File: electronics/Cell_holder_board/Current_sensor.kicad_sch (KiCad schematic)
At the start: 0 parts

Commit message: discord session with Johannes and Fabian, Schematic nearly done, all footprints fields filled
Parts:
- added C1: 220n 25V, Capacitor_SMD:C_0805_2012Metric, symbol Device:C
- added C2: 1n, Capacitor_SMD:C_0805_2012Metric, symbol Device:C
- added J2: Load_connector, TerminalBlock:TerminalBlock_bornier-2_P5.08mm, symbol Connector:Screw_Terminal_01x02
- added U10: ACS712xLCTR-20A, Package_SO:SOIC-8_3.9x4.9mm_P1.27mm, symbol Sensor_Current:ACS712xLCTR-20A
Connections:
- new net: C2.1, U10.6 (FILTER)
- new net +5V: C1.1, U10.8 (VCC)
- new net Current_signal: U10.7 (VIOUT)
- new net GND: C1.2, C2.2, U10.5 (GND)
- new net I_in: J2.2 (Pin_2), U10.1 (IP+), U10.2 (IP+)
- new net I_out: J2.1 (Pin_1), U10.3 (IP-), U10.4 (IP-)
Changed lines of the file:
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@@
 (kicad_sch (version 20230121) (generator eeschema)
   (paper "A4")
+  (wire (pts (xy 82.55 44.45) (xy 87.63 44.45))
+    (stroke (width 0) (type default))
+  )
+  (hierarchical_label "I_in" (shape bidirectional) (at 41.91 39.37 0) (fields_autoplaced)
+    (effects (font (size 1.27 1.27)) (justify left))
+  )
+  (hierarchical_label "I_out" (shape bidirectional) (at 41.91 41.91 0) (fields_autoplaced)
+    (effects (font (size 1.27 1.27)) (justify left))
+  )
+  (hierarchical_label "I_out" (shape bidirectional) (at 62.23 46.99 180) (fields_autoplaced)
+    (effects (font (size 1.27 1.27)) (justify right))
+  )
+  (hierarchical_label "I_in" (shape bidirectional) (at 62.23 36.83 180) (fields_autoplaced)
+    (effects (font (size 1.27 1.27)) (justify right))
+  )
+  (hierarchical_label "Current_signal" (shape output) (at 82.55 41.91 0) (fields_autoplaced)
+    (effects (font (size 1.27 1.27)) (justify left))
+  )
+  (symbol (lib_id "power:GND") (at 72.39 52.07 0) (unit 1)
+    (in_bom yes) (on_board yes) (dnp no) (fields_autoplaced)
+    (property "Reference" "#PWR021" (at 72.39 58.42 0)
+      (effects (font (size 1.27 1.27)) hide)
+    )
+    (property "Value" "GND" (at 72.39 57.15 0)
+      (effects (font (size 1.27 1.27)))
+    )
+    (property "Footprint" "" (at 72.39 52.07 0)
+      (effects (font (size 1.27 1.27)) hide)
+    )
+    (property "Datasheet" "" (at 72.39 52.07 0)
+      (effects (font (size 1.27 1.27)) hide)
+    )
+    (pin "1")
+    (instances
+      (project "Cell_holder_board"
+        (path "/c2697d40-f04f-4888-9ae9-ce0b7f222632/d1e5a9a1-ef5e-4043-b331-33dbe5a7732b"
+          (reference "#PWR021") (unit 1)
+        )
+      )
+    )
+  )
+  (symbol (lib_id "Device:C") (at 87.63 48.26 0) (unit 1)
+    (in_bom yes) (on_board yes) (dnp no) (fields_autoplaced)
+    (property "Reference" "C2" (at 91.44 47.625 0)
+      (effects (font (size 1.27 1.27)) (justify left))
+    )
+    (property "Value" "1n" (at 91.44 50.165 0)
+      (effects (font (size 1.27 1.27)) (justify left))
+    )
+    (property "Footprint" "Capacitor_SMD:C_0805_2012Metric" (at 88.5952 52.07 0)
+      (effects (font (size 1.27 1.27)) hide)
+    )
+    (property "Datasheet" "~" (at 87.63 48.26 0)
+      (effects (font (size 1.27 1.27)) hide)
+    )
+    (pin "1")
+    (pin "2")
+    (instances
+      (project "Cell_holder_board"
+        (path "/c2697d40-f04f-4888-9ae9-ce0b7f222632/d1e5a9a1-ef5e-4043-b331-33dbe5a7732b"
+          (reference "C2") (unit 1)
+        )
+      )
+    )
+  )
+  (symbol (lib_id "Device:C") (at 105.41 41.91 0) (unit 1)
+    (in_bom yes) (on_board yes) (dnp no) (fields_autoplaced)
+    (property "Reference" "C1" (at 109.22 41.275 0)
+      (effects (font (size 1.27 1.27)) (justify left))
+    )
+    (property "Value" "220n 25V" (at 109.22 43.815 0)
+      (effects (font (size 1.27 1.27)) (justify left))
+    )
+    (property "Footprint" "Capacitor_SMD:C_0805_2012Metric" (at 106.3752 45.72 0)
+      (effects (font (size 1.27 1.27)) hide)
+    )
+    (property "Datasheet" "~" (at 105.41 41.91 0)
+      (effects (font (size 1.27 1.27)) hide)
+    )
+    (pin "1")
+    (pin "2")
+    (instances
+      (project "Cell_holder_board"
+        (path "/c2697d40-f04f-4888-9ae9-ce0b7f222632/d1e5a9a1-ef5e-4043-b331-33dbe5a7732b"
+          (reference "C1") (unit 1)
+        )
+      )
+    )
+  )
+  (symbol (lib_id "power:GND") (at 87.63 52.07 0) (unit 1)
+    (in_bom yes) (on_board yes) (dnp no) (fields_autoplaced)
+    (property "Reference" "#PWR023" (at 87.63 58.42 0)
+      (effects (font (size 1.27 1.27)) hide)
+    )
+    (property "Value" "GND" (at 87.63 57.15 0)
+      (effects (font (size 1.27 1.27)))
+    )
+    (property "Footprint" "" (at 87.63 52.07 0)
+      (effects (font (size 1.27 1.27)) hide)
+    )
+    (property "Datasheet" "" (at 87.63 52.07 0)
+      (effects (font (size 1.27 1.27)) hide)
+    )
+    (pin "1")
+    (instances
+      (project "Cell_holder_board"
+        (path "/c2697d40-f04f-4888-9ae9-ce0b7f222632/d1e5a9a1-ef5e-4043-b331-33dbe5a7732b"
+          (reference "#PWR023") (unit 1)
+        )
+      )
+    )
+  )
+  (symbol (lib_id "power:GND") (at 105.41 45.72 0) (unit 1)
+    (in_bom yes) (on_board yes) (dnp no) (fields_autoplaced)
+    (property "Reference" "#PWR025" (at 105.41 52.07 0)
+      (effects (font (size 1.27 1.27)) hide)
+    )
+    (property "Value" "GND" (at 105.41 50.8 0)
+      (effects (font (size 1.27 1.27)))
+    )
+    (property "Footprint" "" (at 105.41 45.72 0)
+      (effects (font (size 1.27 1.27)) hide)
+    )
+    (property "Datasheet" "" (at 105.41 45.72 0)
+      (effects (font (size 1.27 1.27)) hide)
+    )
+    (pin "1")
+    (instances
+      (project "Cell_holder_board"
+        (path "/c2697d40-f04f-4888-9ae9-ce0b7f222632/d1e5a9a1-ef5e-4043-b331-33dbe5a7732b"
+          (reference "#PWR025") (unit 1)
+        )
+      )
+    )
+  )
+  (symbol (lib_id "power:+5V") (at 72.39 31.75 0) (unit 1)
+    (in_bom yes) (on_board yes) (dnp no) (fields_autoplaced)
+    (property "Reference" "#PWR022" (at 72.39 35.56 0)
+      (effects (font (size 1.27 1.27)) hide)
+    )
+    (property "Value" "+5V" (at 72.39 27.94 0)
+      (effects (font (size 1.27 1.27)))
+    )
+    (property "Footprint" "" (at 72.39 31.75 0)
+      (effects (font (size 1.27 1.27)) hide)
+    )
+    (property "Datasheet" "" (at 72.39 31.75 0)
+      (effects (font (size 1.27 1.27)) hide)
+    )
+    (pin "1")
+    (instances
+      (project "Cell_holder_board"
+        (path "/c2697d40-f04f-4888-9ae9-ce0b7f222632/d1e5a9a1-ef5e-4043-b331-33dbe5a7732b"
+          (reference "#PWR022") (unit 1)
+        )
+      )
+    )
+  )
+  (symbol (lib_id "power:+5V") (at 105.41 38.1 0) (unit 1)
+    (in_bom yes) (on_board yes) (dnp no) (fields_autoplaced)
+    (property "Reference" "#PWR024" (at 105.41 41.91 0)
+      (effects (font (size 1.27 1.27)) hide)
+    )
+    (property "Value" "+5V" (at 105.41 34.29 0)
+      (effects (font (size 1.27 1.27)))
+    )
+    (property "Footprint" "" (at 105.41 38.1 0)
+      (effects (font (size 1.27 1.27)) hide)
+    )
+    (property "Datasheet" "" (at 105.41 38.1 0)
+      (effects (font (size 1.27 1.27)) hide)
+    )
+    (pin "1")
+    (instances
+      (project "Cell_holder_board"
+        (path "/c2697d40-f04f-4888-9ae9-ce0b7f222632/d1e5a9a1-ef5e-4043-b331-33dbe5a7732b"
+          (reference "#PWR024") (unit 1)
+        )
+      )
+    )
+  )
+  (symbol (lib_id "Sensor_Current:ACS712xLCTR-20A") (at 72.39 41.91 0) (unit 1)
+    (in_bom yes) (on_board yes) (dnp no) (fields_autoplaced)
+    (property "Reference" "U10" (at 74.3459 30.48 0)
+      (effects (font (size 1.27 1.27)) (justify left))
+    )
+    (property "Value" "ACS712xLCTR-20A" (at 74.3459 33.02 0)
+      (effects (font (size 1.27 1.27)) (justify left))
+    )
+    (property "Footprint" "Package_SO:SOIC-8_3.9x4.9mm_P1.27mm" (at 74.93 50.8 0)
+      (effects (font (size 1.27 1.27) italic) (justify left) hide)
+    )
+    (property "Datasheet" "http://www.allegromicro.com/~/media/Files/Datasheets/ACS712-Datasheet.ashx?la=en" (at 72.39 41.91 0)
+      (effects (font (size 1.27 1.27)) hide)
+    )
+    (pin "1")
+    (pin "2")
+    (pin "3")
+    (pin "4")
+    (pin "5")
+    (pin "6")
+    (pin "7")
+    (pin "8")
+    (instances
+      (project "Cell_holder_board"
+        (path "/c2697d40-f04f-4888-9ae9-ce0b7f222632/d1e5a9a1-ef5e-4043-b331-33dbe5a7732b"
+          (reference "U10") (unit 1)
+        )
+      )
+    )
+  )
+  (symbol (lib_id "Connector:Screw_Terminal_01x02") (at 36.83 41.91 180) (unit 1)
+    (in_bom yes) (on_board yes) (dnp no)
+    (property "Reference" "J2" (at 36.83 34.29 0)
+      (effects (font (size 1.27 1.27)))
+    )
+    (property "Value" "Load_connector" (at 34.29 40.64 90)
+      (effects (font (size 1.27 1.27)))
+    )
+    (property "Footprint" "TerminalBlock:TerminalBlock_bornier-2_P5.08mm" (at 36.83 41.91 0)
+      (effects (font (size 1.27 1.27)) hide)
+    )
+    (property "Datasheet" "~" (at 36.83 41.91 0)
+      (effects (font (size 1.27 1.27)) hide)
+    )
+    (pin "1")
+    (pin "2")
+    (instances
+      (project "Cell_holder_board"
+        (path "/c2697d40-f04f-4888-9ae9-ce0b7f222632"
+          (reference "J2") (unit 1)
+        )
+        (path "/c2697d40-f04f-4888-9ae9-ce0b7f222632/d1e5a9a1-ef5e-4043-b331-33dbe5a7732b"
+          (reference "J3") (unit 1)
+        )
+      )
+    )
+  )
 )

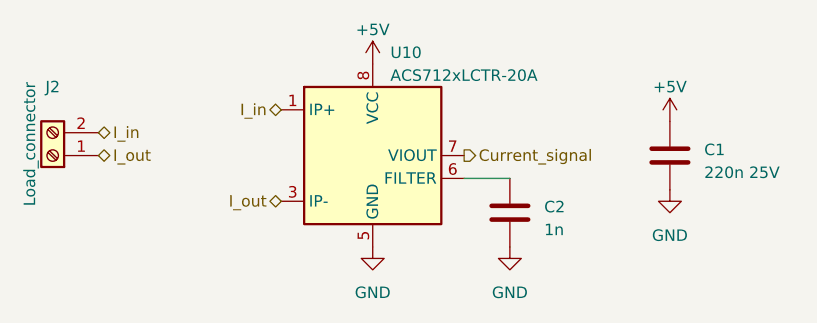
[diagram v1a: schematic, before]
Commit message: finished layout of cell_holder_board
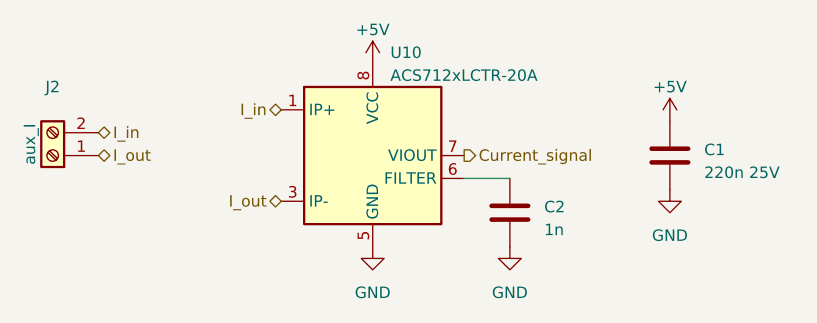
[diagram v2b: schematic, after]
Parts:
- J2: value Load_connector -> aux_I
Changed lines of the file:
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@@
       (effects (font (size 1.27 1.27)))
     )
-    (property "Value" "Load_connector" (at 34.29 40.64 90)
+    (property "Value" "aux_I" (at 34.29 40.64 90)
       (effects (font (size 1.27 1.27)))
     )
